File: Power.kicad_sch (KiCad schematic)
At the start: 19 parts, among them J1 Jack-DC, J2 USB_B_Micro, U1 LM2596S-5, U3 LM1117-3.3, U4 LM1117-1.8

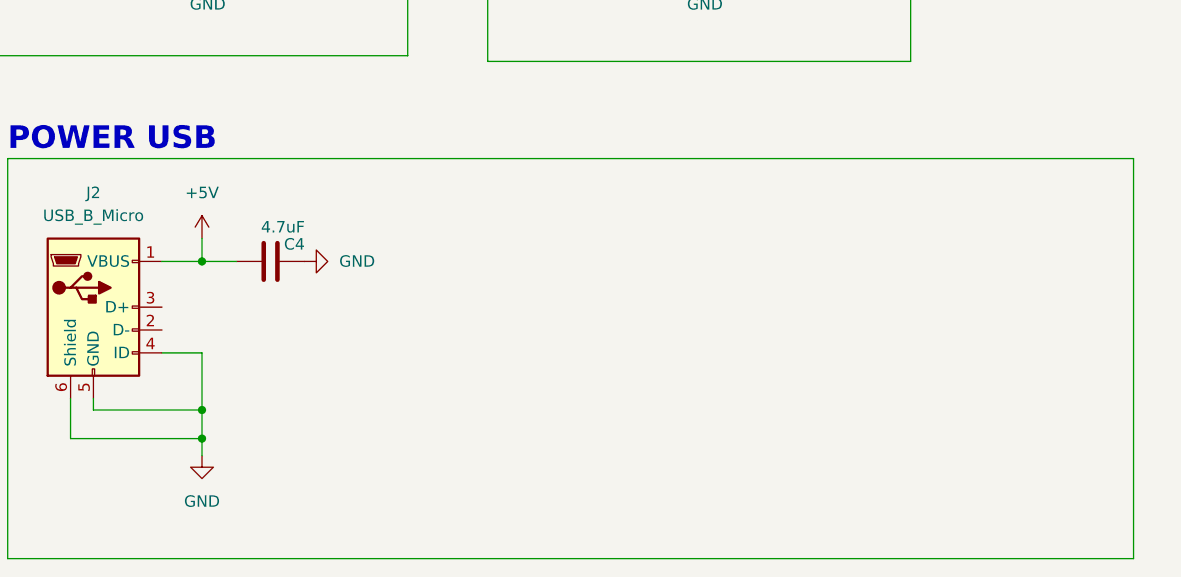
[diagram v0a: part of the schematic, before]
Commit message: USB Power switch eklendi. Devresi tamamlanacak
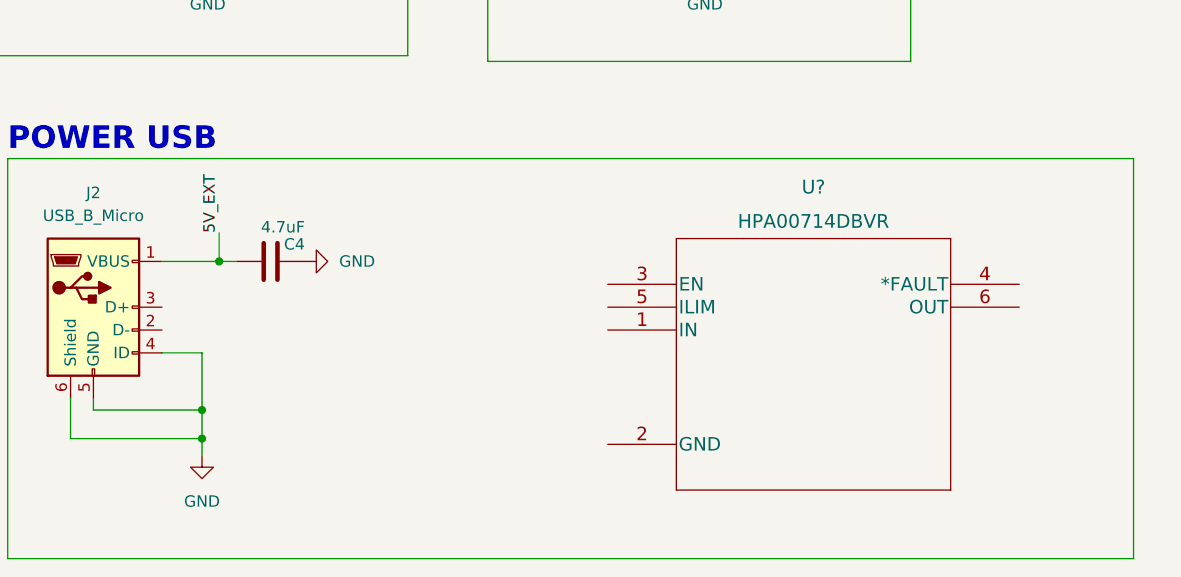
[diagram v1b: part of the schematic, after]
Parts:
- added U?: HPA00714DBVR, erkan-hw-lib:HPA00714DBVR, symbol erkan-hw:HPA00714DBVR
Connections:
- net +5V: no longer C4.1, J2.1 (VBUS)
- new net 5V_EXT: C4.1, J2.1 (VBUS)
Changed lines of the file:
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@@
 (kicad_sch (version 20211123) (generator eeschema)
   (paper "A4")
-  (junction (at 48.26 143.51) (diameter 0) (color 0 0 0 0)
+  (junction (at 50.165 143.51) (diameter 0) (color 0 0 0 0)
   )
   (junction (at 35.56 35.56) (diameter 0) (color 0 0 0 0)
@@
     (stroke (width 0.5) (type default) (color 57 87 255 1))
   )
+  (wire (pts (xy 50.165 140.335) (xy 50.165 143.51))
+    (stroke (width 0) (type default) (color 0 0 0 0))
+  )
   (wire (pts (xy 24.13 26.035) (xy 130.175 26.035))
     (stroke (width 0.5) (type default) (color 57 87 255 1))
@@
     (stroke (width 0) (type default) (color 0 0 0 0))
   )
-  (wire (pts (xy 43.815 143.51) (xy 48.26 143.51))
+  (wire (pts (xy 43.815 143.51) (xy 50.165 143.51))
     (stroke (width 0) (type default) (color 0 0 0 0))
   )
@@
     (stroke (width 0) (type default) (color 0 0 0 0))
   )
-  (wire (pts (xy 48.26 143.51) (xy 48.26 140.97))
-    (stroke (width 0) (type default) (color 0 0 0 0))
-  )
   (wire (pts (xy 116.84 89.535) (xy 116.84 95.885))
     (stroke (width 0) (type default) (color 0 0 0 0))
@@
     (stroke (width 0.5) (type default) (color 57 87 255 1))
   )
+  (wire (pts (xy 50.165 143.51) (xy 52.07 143.51))
+    (stroke (width 0) (type default) (color 0 0 0 0))
+  )
   (wire (pts (xy 111.76 89.535) (xy 116.84 89.535))
     (stroke (width 0) (type default) (color 0 0 0 0))
@@
   (wire (pts (xy 26.67 132.08) (xy 26.67 176.53))
     (stroke (width 0.5) (type default) (color 57 87 255 1))
-  )
-  (wire (pts (xy 48.26 143.51) (xy 52.07 143.51))
-    (stroke (width 0) (type default) (color 0 0 0 0))
   )
   (wire (pts (xy 26.67 132.08) (xy 151.765 132.08))
@@
   (text "POWER JACK - 24V" (at 152.4 25.4 0)
     (effects (font (size 2.5 2.5) (thickness 0.5) bold) (justify left bottom))
+  )
+  (label "5V_EXT" (at 50.165 140.335 90)
+    (effects (font (size 1.27 1.27)) (justify left bottom))
   )
   (global_label "V_IN" (shape input) (at 266.7 37.465 0) (fields_autoplaced)
@@
     (pin "3")
   )
+  (symbol (lib_id "erkan-hw:HPA00714DBVR") (at 93.345 146.05 0) (unit 1)
+    (in_bom yes) (on_board yes) (fields_autoplaced)
+    (property "Reference" "U?" (id 0) (at 116.205 135.255 0)
+      (effects (font (size 1.524 1.524)))
+    )
+    (property "Value" "HPA00714DBVR" (id 1) (at 116.205 139.065 0)
+      (effects (font (size 1.524 1.524)))
+    )
+    (property "Footprint" "erkan-hw-lib:HPA00714DBVR" (id 2) (at 116.205 139.954 0)
+      (effects (font (size 1.524 1.524)) hide)
+    )
+    (property "Datasheet" "" (id 3) (at 93.345 146.05 0)
+      (effects (font (size 1.524 1.524)))
+    )
+    (pin "1")
+    (pin "2")
+    (pin "3")
+    (pin "4")
+    (pin "5")
+    (pin "6")
+  )
   (symbol (lib_id "Connector:TestPoint") (at 262.89 56.515 90) (mirror x) (unit 1)
     (in_bom yes) (on_board yes)
@@
       (effects (font (size 1.27 1.27)) hide)
     )
-    (pin "1")
-  )
-  (symbol (lib_id "power:+5V") (at 48.26 140.97 0) (unit 1)
-    (in_bom yes) (on_board yes) (fields_autoplaced)
-    (property "Reference" "#PWR01" (id 0) (at 48.26 144.78 0)
-      (effects (font (size 1.27 1.27)) hide)
-    )
-    (property "Value" "+5V" (id 1) (at 48.26 135.89 0))
-    (property "Footprint" "" (id 2) (at 48.26 140.97 0)
-      (effects (font (size 1.27 1.27)) hide)
-    )
-    (property "Datasheet" "" (id 3) (at 48.26 140.97 0)
-      (effects (font (size 1.27 1.27)) hide)
-    )

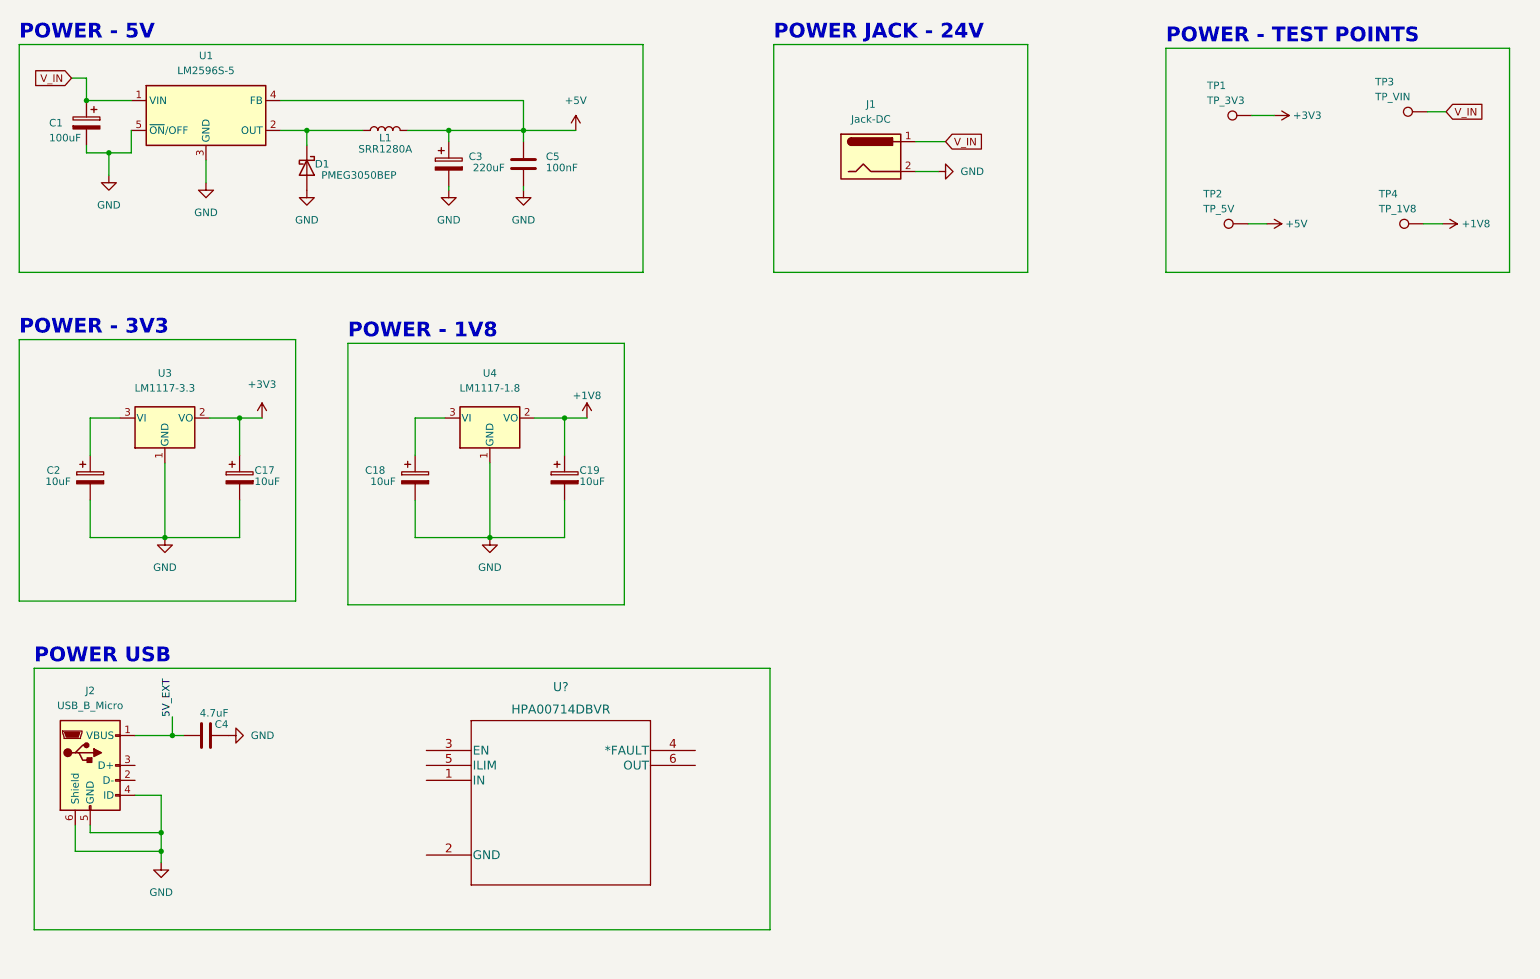
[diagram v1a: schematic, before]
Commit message: LM2596 Layout oluşturuldu, USB Power switch tarafı eksik
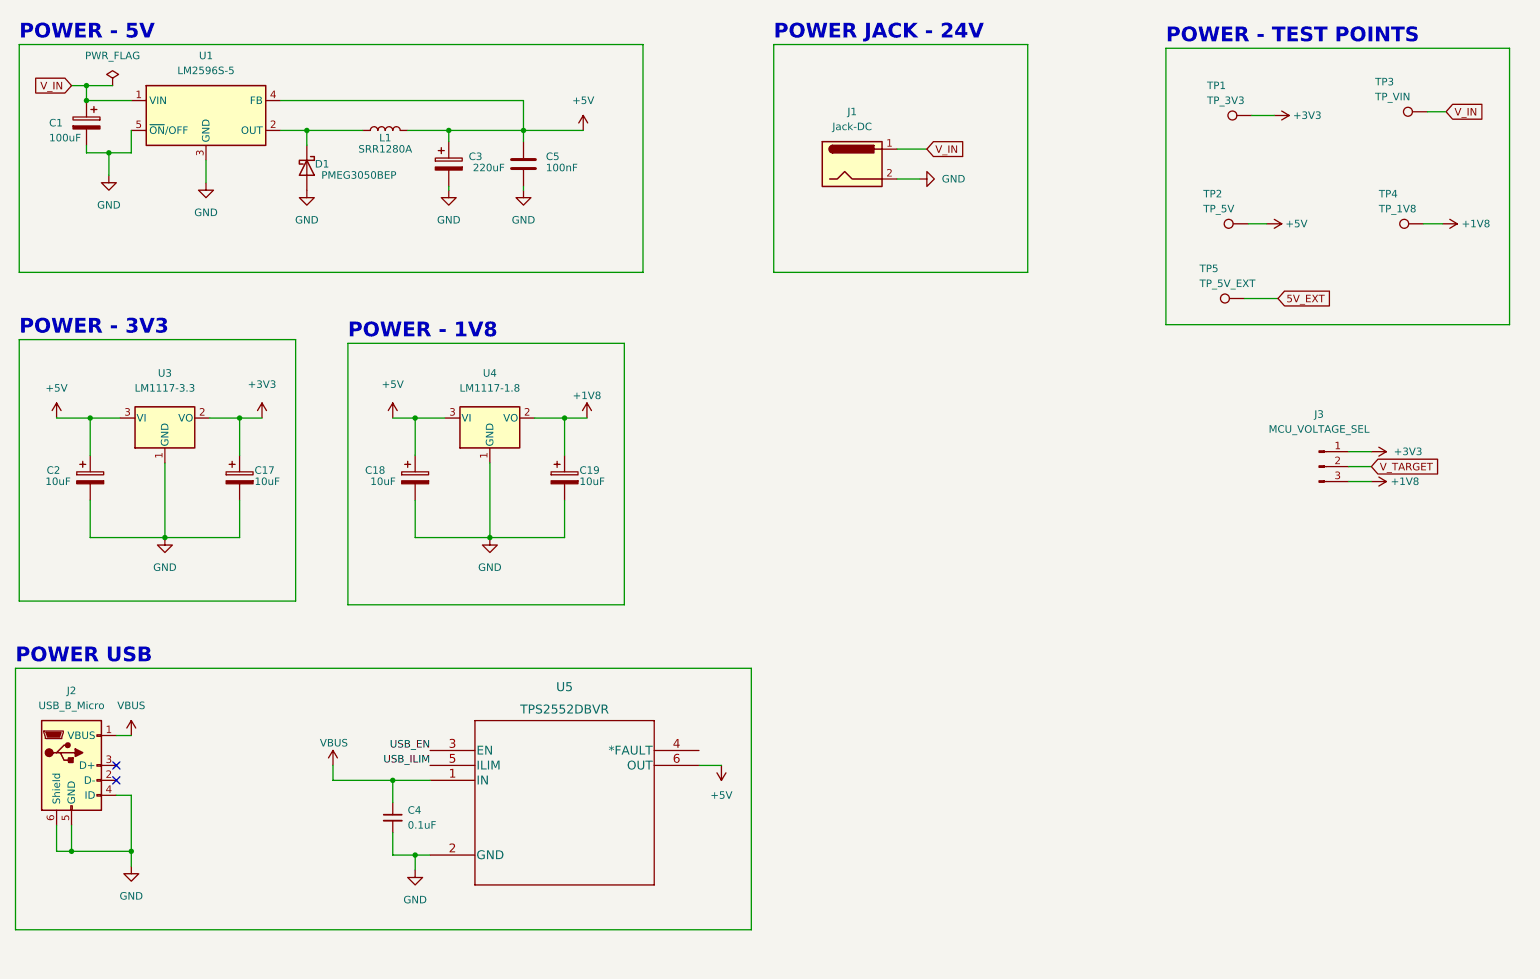
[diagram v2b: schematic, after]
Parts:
- removed C4: 4.7uF, Capacitor_SMD:C_0805_2012Metric, symbol Device:C
- removed U?: HPA00714DBVR, erkan-hw-lib:HPA00714DBVR, symbol erkan-hw:HPA00714DBVR
- added C4: 0.1uF, symbol Device:C_Small
- added J3: MCU_VOLTAGE_SEL, Connector_PinHeader_2.54mm:PinHeader_1x03_P2.54mm_Vertical, symbol Connector:Conn_01x03_Male
- added TP5: TP_5V_EXT, TestPoint:TestPoint_Pad_D1.0mm, symbol Connector:TestPoint
- added U5: TPS2552DBVR, erkan-hw-lib:TPS2552DBVR, symbol erkan-hw:TPS2552DBVR
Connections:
- net +1V8: now also J3.3 (Pin_3)
- net +3V3: now also J3.1 (Pin_1)
- net +5V: now also C18.1, C2.1, U3.3 (VI), U4.3 (VI), U5.6 (OUT)
- net 5V_EXT: now also TP5.1; no longer J2.1 (VBUS)
- net GND: now also C4.2, U5.2 (GND)
- new net USB_EN: U5.3 (EN)
- new net USB_ILIM: U5.5 (ILIM)
- new net VBUS: C4.1, J2.1 (VBUS), U5.1 (IN)
- new net V_TARGET: J3.2 (Pin_2)
- no-connect marks 0 -> 2
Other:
- moved on the sheet: J1, J2

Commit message: LM2596 Layout ve yollar çizildi
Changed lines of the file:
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@@
   (junction (at 109.855 40.64) (diameter 0) (color 0 0 0 0)
+  )
+  (junction (at 114.3 40.64) (diameter 0) (color 0 0 0 0)
   )
   (junction (at 39.37 44.45) (diameter 0) (color 0 0 0 0)
@@
     (stroke (width 0) (type default) (color 0 0 0 0))
   )
-  (wire (pts (xy 68.58 35.56) (xy 109.855 35.56))
+  (wire (pts (xy 68.58 35.56) (xy 114.3 35.56))
     (stroke (width 0) (type default) (color 0 0 0 0))
   )
@@
     (stroke (width 0) (type default) (color 0 0 0 0))
   )
-  (wire (pts (xy 109.855 40.64) (xy 120.015 40.64))
-    (stroke (width 0) (type default) (color 0 0 0 0))
-  )
   (wire (pts (xy 130.175 26.035) (xy 130.175 64.77))
     (stroke (width 0.5) (type solid) (color 57 87 255 1))
@@
     (stroke (width 0) (type default) (color 0 0 0 0))
   )
-  (wire (pts (xy 109.855 35.56) (xy 109.855 40.64))
+  (wire (pts (xy 114.3 35.56) (xy 114.3 40.64))
     (stroke (width 0) (type default) (color 0 0 0 0))
   )
@@
     (stroke (width 0.5) (type solid) (color 57 87 255 1))
   )
+  (wire (pts (xy 114.3 40.64) (xy 120.015 40.64))
+    (stroke (width 0) (type default) (color 0 0 0 0))
+  )
   (wire (pts (xy 254 95.25) (xy 250.19 95.25))
     (stroke (width 0) (type default) (color 0 0 0 0))
@@
     (stroke (width 0) (type default) (color 0 0 0 0))
   )
+  (wire (pts (xy 114.3 40.64) (xy 109.855 40.64))
+    (stroke (width 0) (type default) (color 0 0 0 0))
+  )

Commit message: LM2596 layout değiştirildi
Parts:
- added D? (x4): LED, symbol Device:LED
- added R? (x4): 1.2k, symbol Device:R_Small_US
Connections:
- net +1V8: now also R?.2
- net +3V3: now also R?.2
- net +5V: now also R?.2
- net GND: now also D?.1 (K), D?.1 (K), D?.1 (K), D?.1 (K)
- net V_IN: now also R?.2
- new net: D?.2 (A), R?.1 (x4)
- no-connect marks 2 -> 3
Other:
- moved on the sheet: J3
